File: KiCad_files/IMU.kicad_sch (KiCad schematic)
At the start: 12 parts, among them U13 BNO085

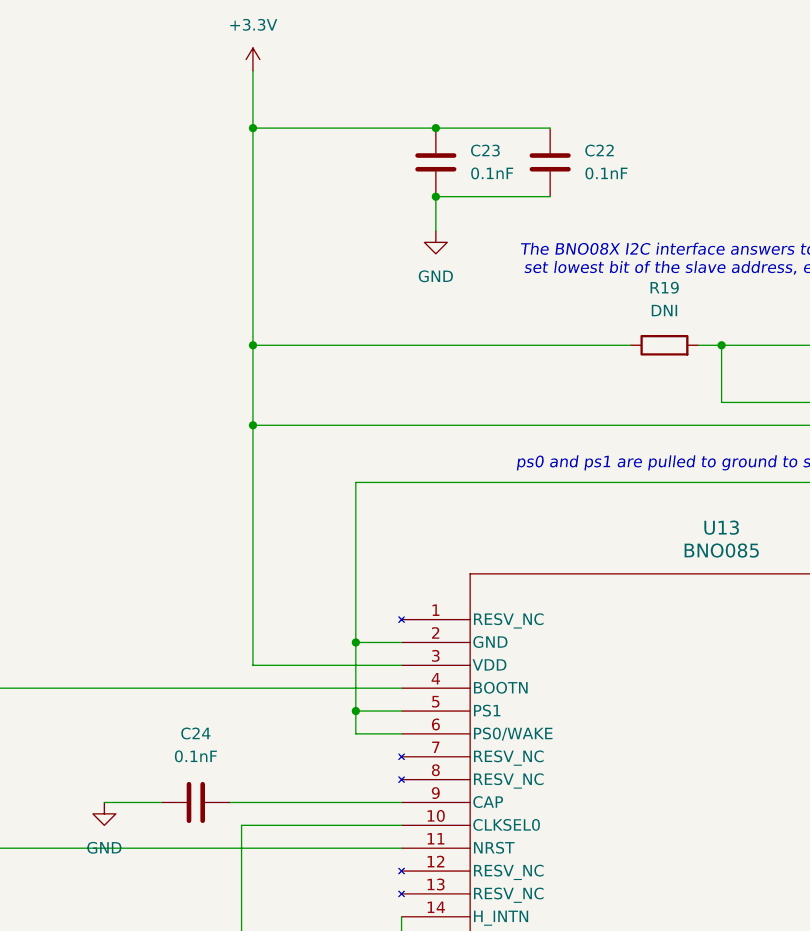
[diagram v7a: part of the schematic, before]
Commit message: footprinttejä komponenteille + kapasitanssit korjattu imusta
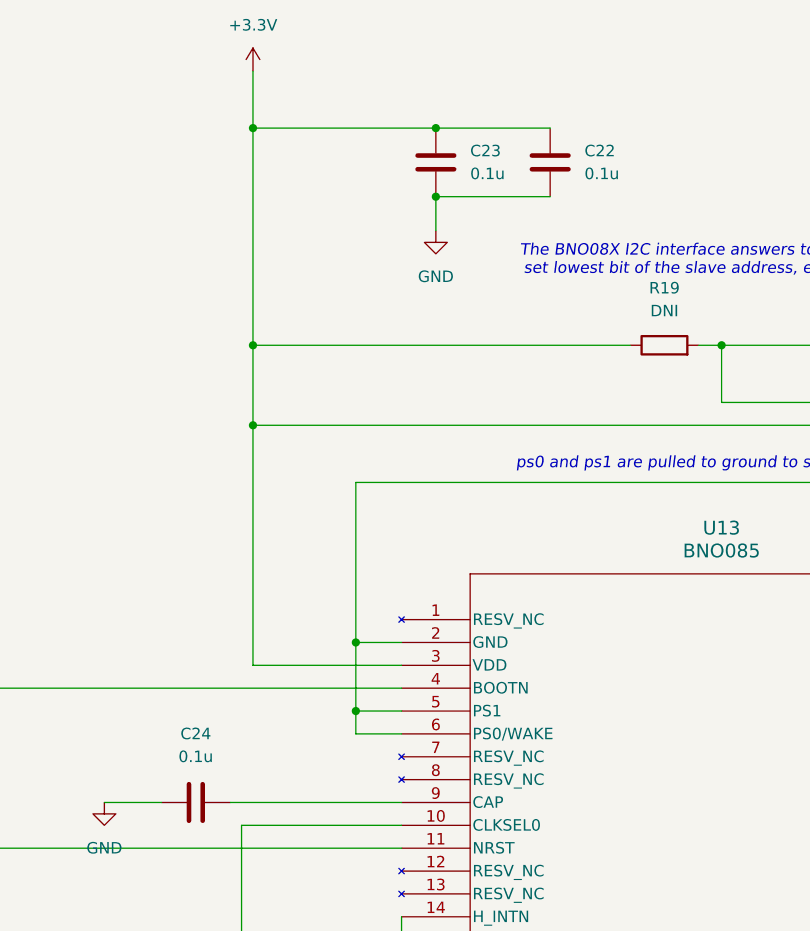
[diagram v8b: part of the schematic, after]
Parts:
- C22, C23, C24: value 0.1nF -> 0.1u; footprint (none) -> Capacitor_SMD:C_0805_2012Metric_Pad1.18x1.45mm_HandSolder
- R16, R17, R18, R19, R20, R21, R22, R23: footprint (none) -> Resistor_SMD:R_0805_2012Metric_Pad1.20x1.40mm_HandSolder
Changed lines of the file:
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@@
 			)
 		)
-		(property "Footprint" ""
+		(property "Footprint" "Resistor_SMD:R_0805_2012Metric_Pad1.20x1.40mm_HandSolder"
 			(at 54.102 102.87 90)
 			(effects
@@
 			)
 		)
-		(property "Value" "0.1nF"
+		(property "Value" "0.1u"
 			(at 139.7 33.0199 0)
 			(effects
@@
 			)
 		)
-		(property "Footprint" ""
+		(property "Footprint" "Capacitor_SMD:C_0805_2012Metric_Pad1.18x1.45mm_HandSolder"
 			(at 136.8552 35.56 0)
 			(effects
@@
 			)
 		)
-		(property "Footprint" ""
+		(property "Footprint" "Resistor_SMD:R_0805_2012Metric_Pad1.20x1.40mm_HandSolder"
 			(at 35.052 102.87 90)
 			(effects
@@
 			)
 		)
-		(property "Footprint" ""
+		(property "Footprint" "Resistor_SMD:R_0805_2012Metric_Pad1.20x1.40mm_HandSolder"
 			(at 236.982 105.41 90)
 			(effects
@@
 			)
 		)
-		(property "Footprint" ""
+		(property "Footprint" "Resistor_SMD:R_0805_2012Metric_Pad1.20x1.40mm_HandSolder"
 			(at 66.04 97.028 90)
 			(effects
@@
 			)
 		)
-		(property "Footprint" ""
+		(property "Footprint" "Resistor_SMD:R_0805_2012Metric_Pad1.20x1.40mm_HandSolder"
 			(at 45.212 102.87 90)
 			(effects
@@
 			)
 		)
-		(property "Footprint" ""
+		(property "Footprint" "Resistor_SMD:R_0805_2012Metric_Pad1.20x1.40mm_HandSolder"
 			(at 148.59 53.848 90)
 			(effects
@@
 			)
 		)
-		(property "Footprint" ""
+		(property "Footprint" "Resistor_SMD:R_0805_2012Metric_Pad1.20x1.40mm_HandSolder"
 			(at 247.142 105.41 90)
 			(effects
@@
 			)
 		)
-		(property "Value" "0.1nF"
+		(property "Value" "0.1u"
 			(at 127 33.0199 0)
 			(effects
@@
 			)
 		)
-		(property "Footprint" ""
+		(property "Footprint" "Capacitor_SMD:C_0805_2012Metric_Pad1.18x1.45mm_HandSolder"
 			(at 124.1552 35.56 0)
 			(effects
@@
 			)
 		)
-		(property "Footprint" ""
+		(property "Footprint" "Resistor_SMD:R_0805_2012Metric_Pad1.20x1.40mm_HandSolder"
 			(at 170.18 53.848 90)
 			(effects
@@
 			)
 		)
-		(property "Value" "0.1nF"
+		(property "Value" "0.1u"
 			(at 96.52 97.79 90)
 			(effects
@@
 			)
 		)
-		(property "Footprint" ""
+		(property "Footprint" "Capacitor_SMD:C_0805_2012Metric_Pad1.18x1.45mm_HandSolder"
 			(at 92.71 103.8352 0)
 			(effects
